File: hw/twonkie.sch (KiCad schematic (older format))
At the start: 52 parts, among them J1 DX07P024AJ1R1500, J2 690-024-294T331, J3 629105150521, Q1 BSD840N, Q2 BSD840N, Q3 BSD840N, SW1 EVQ-P7M01P, U1 INA260, U2 INA260, U3 MIC5504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

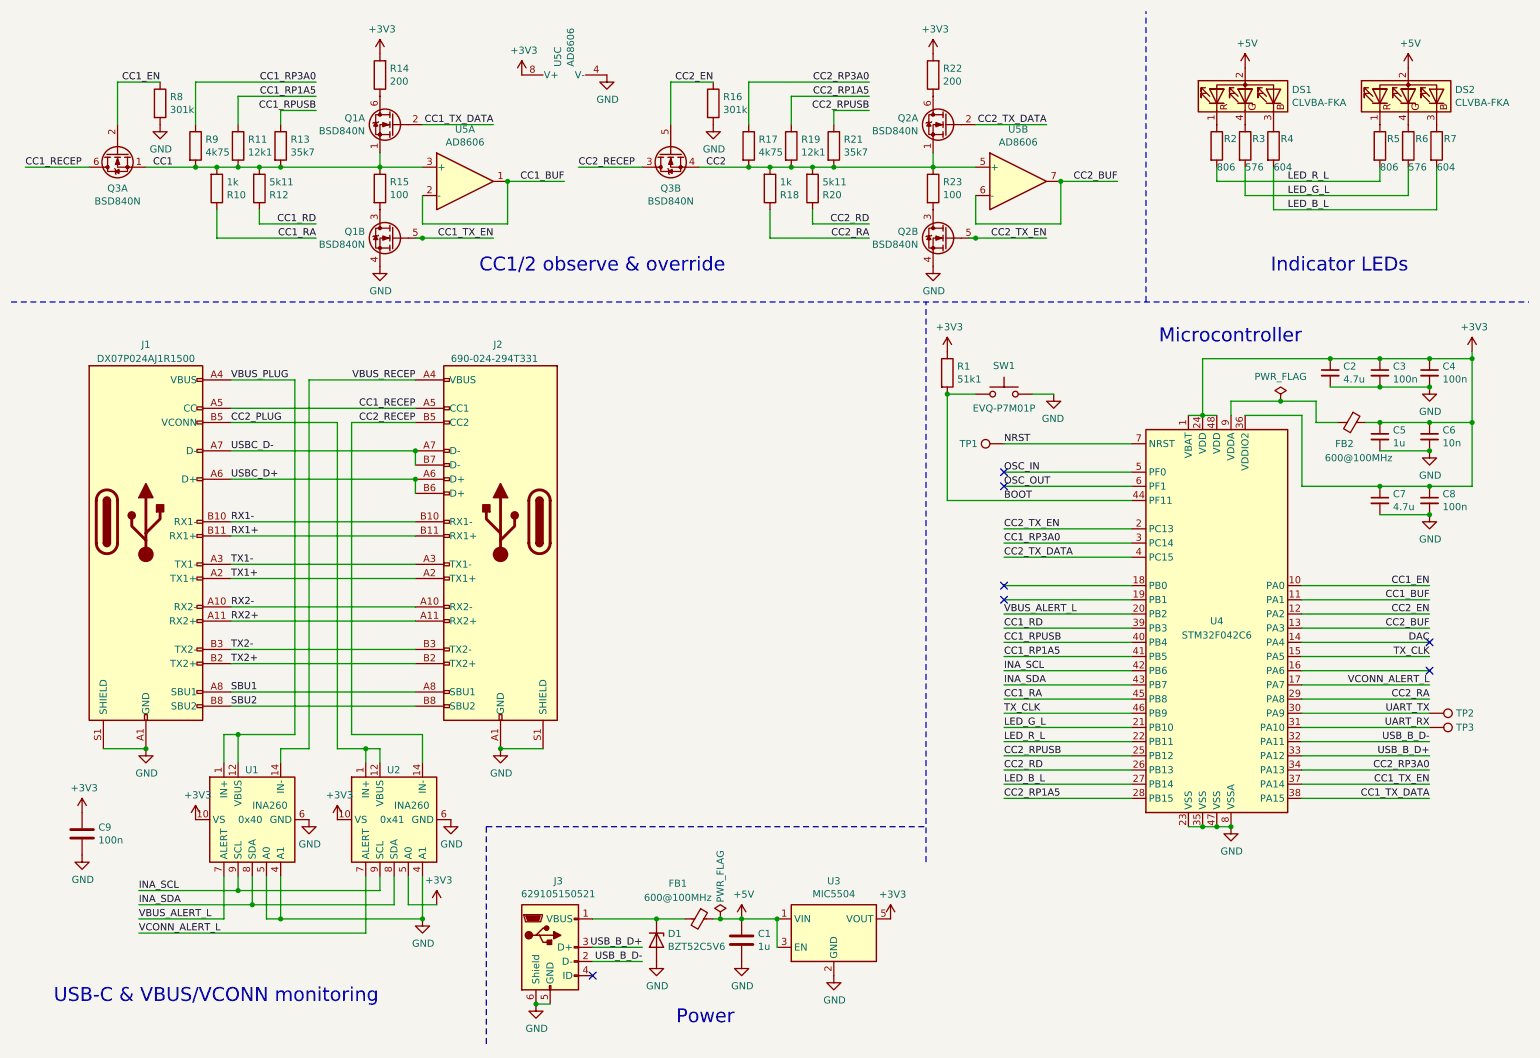
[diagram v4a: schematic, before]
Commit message: Many reworks based on David's and Vincent's feedback
* The USB plug wouldn't straddle a 1.6mm board, so switched to
  a different one
* Redid the USB section to make room for the new plug
* Twinkie firmware needs some special pin functions I wasn't aware
  of, so some signals had to be moved to different pins
* Misc other tweaks like merging resistor values
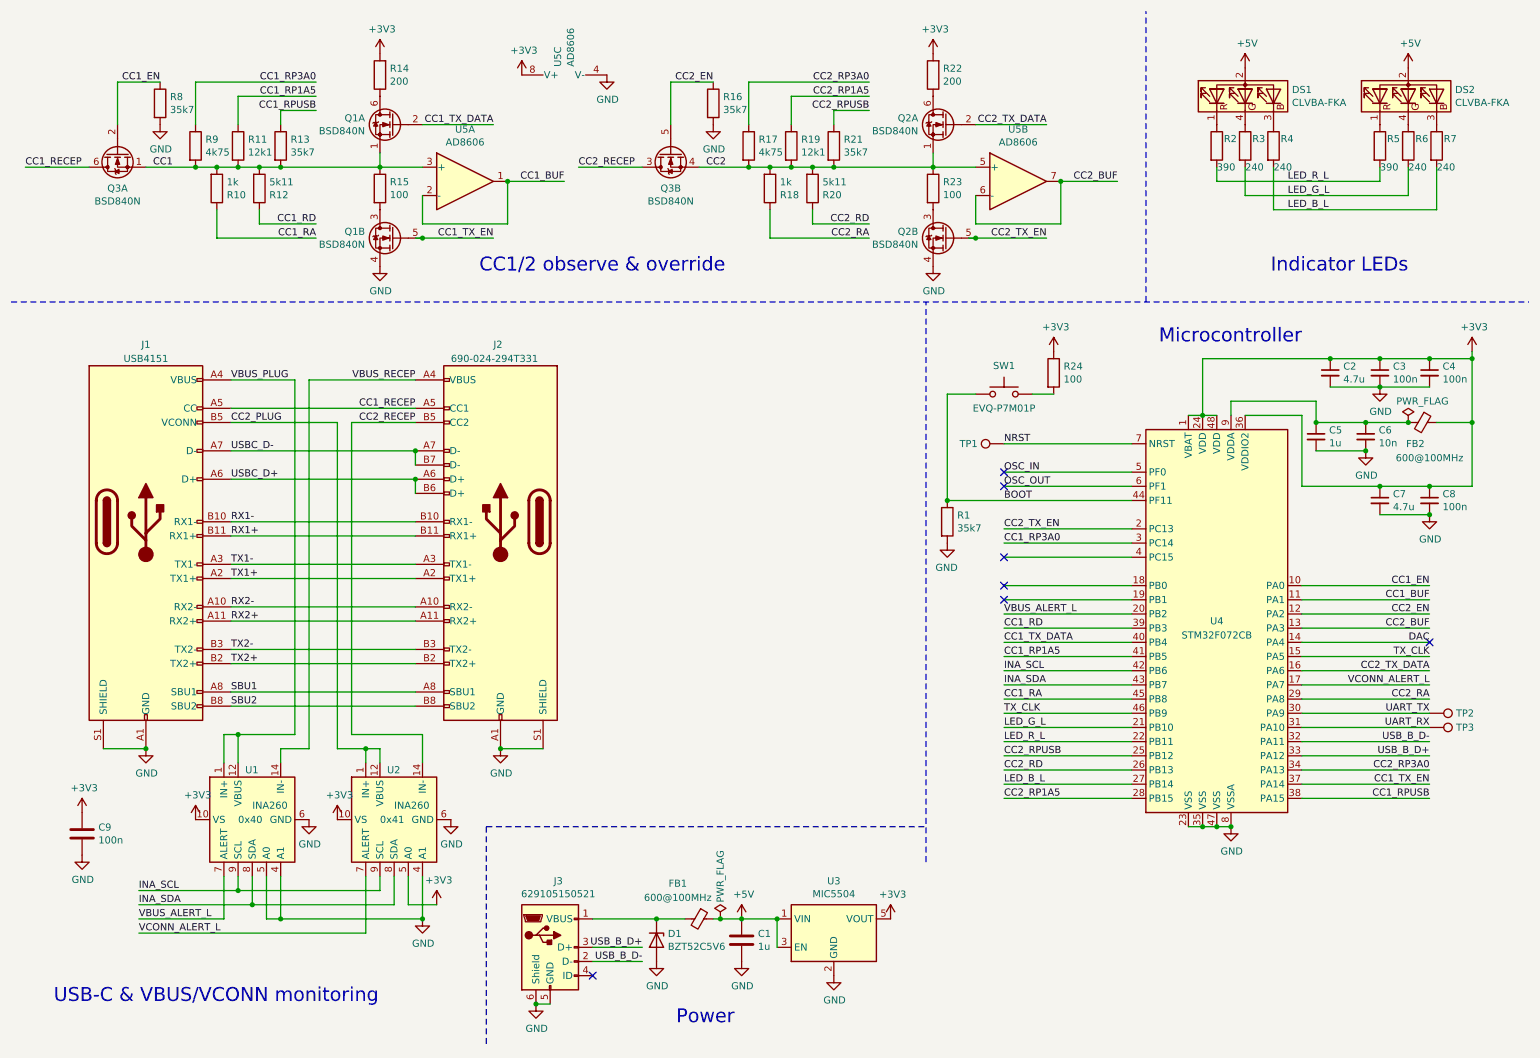
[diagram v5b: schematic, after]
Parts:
- added R24: 100, Resistor_SMD:R_0402_1005Metric_Pad0.72x0.64mm_HandSolder, symbol Device:R
- J1: value DX07P024AJ1R1500 -> USB4151; footprint twonkie:JAE_DX07P024AJ1R1500 -> twonkie:GCT_USB4151_EdgeMount; DigiKey P/N 670-2868-1-ND -> 2073-USB4151-GF-CCT-ND; Manufacturer JAE -> GCT; Mfg P/N DX07P024AJ1R1500 -> USB4151-GF-C
- R1: value 51k1 -> 35k7; DigiKey P/N 311-51.1KLRCT-ND -> 311-35.7KLRCT-ND; Mfg P/N RC0402FR-0751K1L -> RC0402FR-0735K7L
- R13, R21: DigiKey P/N (none) -> 311-35.7KLRCT-ND
- R16, R8: value 301k -> 35k7; DigiKey P/N 311-301KLRCT-ND -> 311-35.7KLRCT-ND; Mfg P/N RC0402FR-07301KL -> RC0402FR-0735K7L
- R2, R5: value 806 -> 390
- R3, R6: value 576 -> 240; DigiKey P/N YAG3189CT-ND -> (none); Mfg P/N RC0402FR-07576RL -> RC0402FR-07240RL
- R4, R7: value 604 -> 240; DigiKey P/N YAG3199CT-ND -> (none); Mfg P/N RC0402FR-07604RL -> RC0402FR-07240RL
- U4: value STM32F042C6 -> STM32F072CB
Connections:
- net +3V3: now also R24.1; no longer C5.1, C6.1, R1.1
- net BOOT: now also R1.1; no longer R1.2
- net CC1_RPUSB: now also U4.38 (PA15); no longer U4.40 (PB4)
- net CC1_TX_DATA: now also U4.40 (PB4); no longer U4.38 (PA15)
- net CC2_TX_DATA: now also U4.16 (PA6); no longer U4.4 (PC15)
- net GND: now also R1.2; no longer SW1.1
- net at FB2.2, U4.9 (VDDA): now also C5.1, C6.1
- new net: R24.2, SW1.1
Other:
- moved on the sheet: C5, C6, FB2, R1

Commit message: v0.99 with fabrication files
* Switch USB-MicroB receptacle to version with drill slots
* Expand VBUS connections on USB-C plug
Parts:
- J3: footprint Connector_USB:USB_Micro-B_Wuerth_629105150521_CircularHoles -> Connector_USB:USB_Micro-B_Wuerth_629105150521
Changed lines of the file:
@@
 F 0 "J3" H 4357 7567 50  0000 C CNN
 F 1 "629105150521" H 4357 7476 50  0000 C CNN
-F 2 "Connector_USB:USB_Micro-B_Wuerth_629105150521_CircularHoles" H 4450 7050 50  0001 C CNN
+F 2 "Connector_USB:USB_Micro-B_Wuerth_629105150521" H 4450 7050 50  0001 C CNN
 F 3 "~" H 4450 7050 50  0001 C CNN
 F 4 "732-5960-1-ND" H 4300 7100 50  0001 C CNN "DigiKey P/N"

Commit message: First batch of v1.0 fixes
* Restore QFN/TQFP combo footprint for U4, make sure it stays
* Grow some VBUS copper pours
* Make U4 decap ground connections less solid for better soldering
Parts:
- U4: footprint Package_QFP:LQFP-48_7x7mm_P0.5mm -> twonkie:LQFP-48_7x7mm_P0.5mm-QFN48-Frankenstein
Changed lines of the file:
@@
 F 0 "U4" H 9000 4700 50  0000 C CNN
 F 1 "STM32F072CB" H 9000 4600 50  0000 C CNN
-F 2 "Package_QFP:LQFP-48_7x7mm_P0.5mm" H 8500 3350 50  0001 R CNN
+F 2 "twonkie:LQFP-48_7x7mm_P0.5mm-QFN48-Frankenstein" H 8500 3350 50  0001 R CNN
 F 3 "https://www.analog.com/media/en/technical-documentation/data-sheets/AD8610_8620.pdf" H 9000 4750 50  0001 C CNN
 F 4 "497-19319-1-ND" H 9000 4750 50  0001 C CNN "DigiKey P/N"

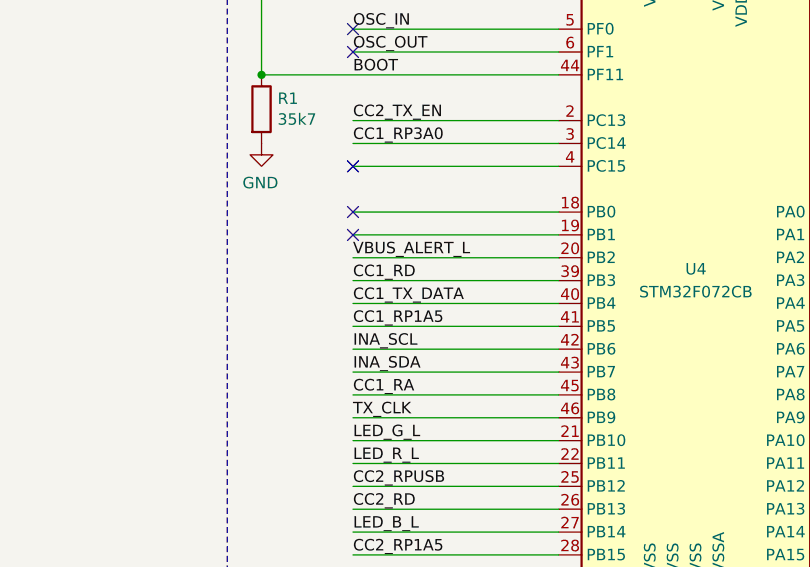
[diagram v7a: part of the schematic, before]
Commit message: Add I2C pullup resistors
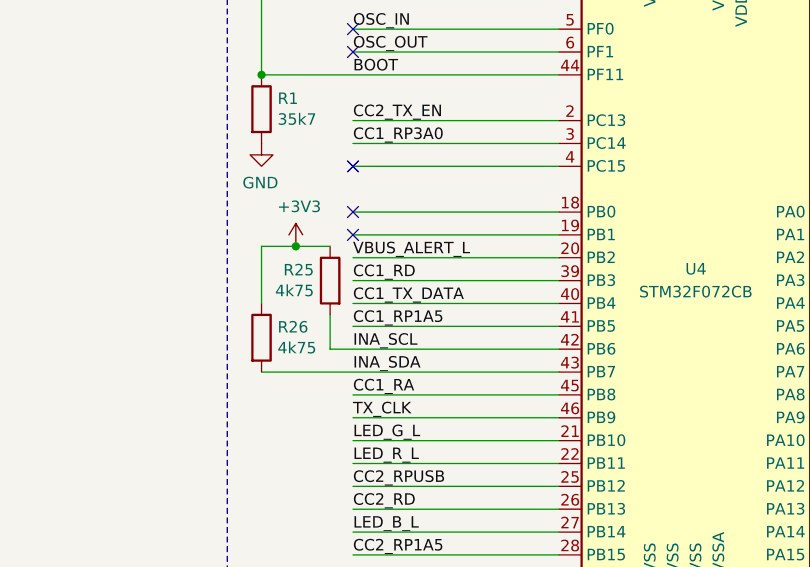
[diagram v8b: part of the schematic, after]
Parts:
- added R25, R26: 4k75, Resistor_SMD:R_0402_1005Metric_Pad0.72x0.64mm_HandSolder, symbol Device:R
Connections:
- net +3V3: now also R25.1, R26.1
- net INA_SCL: now also R25.2
- net INA_SDA: now also R26.2
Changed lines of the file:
@@
 Wire Wire Line
 	7500 5050 8400 5050
-Wire Wire Line
-	8400 5150 7500 5150
-Wire Wire Line
-	7500 5250 8400 5250
 Text Label 7500 4950 0    50   ~ 0
 CC1_TX_DATA
@@
 	1    0    0    -1
 $EndComp
+$Comp
+L Device:R R25
+U 1 1 5FEB3ABD
+P 7400 4850
+F 0 "R25" H 7470 4896 50  0000 L CNN
+F 1 "4k75" H 7470 4805 50  0000 L CNN
+F 2 "Resistor_SMD:R_0402_1005Metric_Pad0.72x0.64mm_HandSolder" V 7330 4850 50  0001 C CNN
+F 3 "~" H 7400 4850 50  0001 C CNN
+F 4 "311-4.75KLCT-ND" H 7400 4850 50  0001 C CNN "DigiKey P/N"
+F 5 "RC0402FR-074K75L" H 7400 4850 50  0001 C CNN "Mfg P/N"
+F 6 "Yageo" H 7400 4850 50  0001 C CNN "Manufacturer"
+	1    7400 4850
+	-1   0    0    -1
+$EndComp
+$Comp
+L Device:R R26
+U 1 1 5FEB4E56
+P 7100 5100
+F 0 "R26" H 7170 5146 50  0000 L CNN
+F 1 "4k75" H 7170 5055 50  0000 L CNN
+F 2 "Resistor_SMD:R_0402_1005Metric_Pad0.72x0.64mm_HandSolder" V 7030 5100 50  0001 C CNN
+F 3 "~" H 7100 5100 50  0001 C CNN
+F 4 "311-4.75KLCT-ND" H 7100 5100 50  0001 C CNN "DigiKey P/N"
+F 5 "RC0402FR-074K75L" H 7100 5100 50  0001 C CNN "Mfg P/N"
+F 6 "Yageo" H 7100 5100 50  0001 C CNN "Manufacturer"
+	1    7100 5100
+	1    0    0    -1
+$EndComp
+$Comp
+L power:+3V3 #PWR03
+U 1 1 5FEDF16F
+P 7250 4700
+F 0 "#PWR03" H 7250 4550 50  0001 C CNN
+F 1 "+3V3" H 7265 4873 50  0000 C CNN
+F 2 "" H 7250 4700 50  0001 C CNN
+F 3 "" H 7250 4700 50  0001 C CNN
+	1    7250 4700
+	1    0    0    -1
+$EndComp
+Wire Wire Line
+	7250 4700 7400 4700
+Wire Wire Line
+	7250 4700 7100 4700
+Wire Wire Line
+	7100 4700 7100 4950
+Connection ~ 7250 4700
+Wire Wire Line
+	7400 5000 7400 5150
+Wire Wire Line
+	7400 5150 8400 5150
+Wire Wire Line
+	7100 5250 8400 5250
 $EndSCHEMATC
